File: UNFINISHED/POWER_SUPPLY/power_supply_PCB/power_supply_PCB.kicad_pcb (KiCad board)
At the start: 2 copper layers, 50 x 80 mm, 22 parts, among them J1 AC INPUT 12+12 1.5A, J2 OUT1, J3 OUT2, J4 OUT3, J5 OUT4, J6 OUT5, J7 OUT6, J8 OUT7, J9 OUT8, U1 LM7812_TO220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

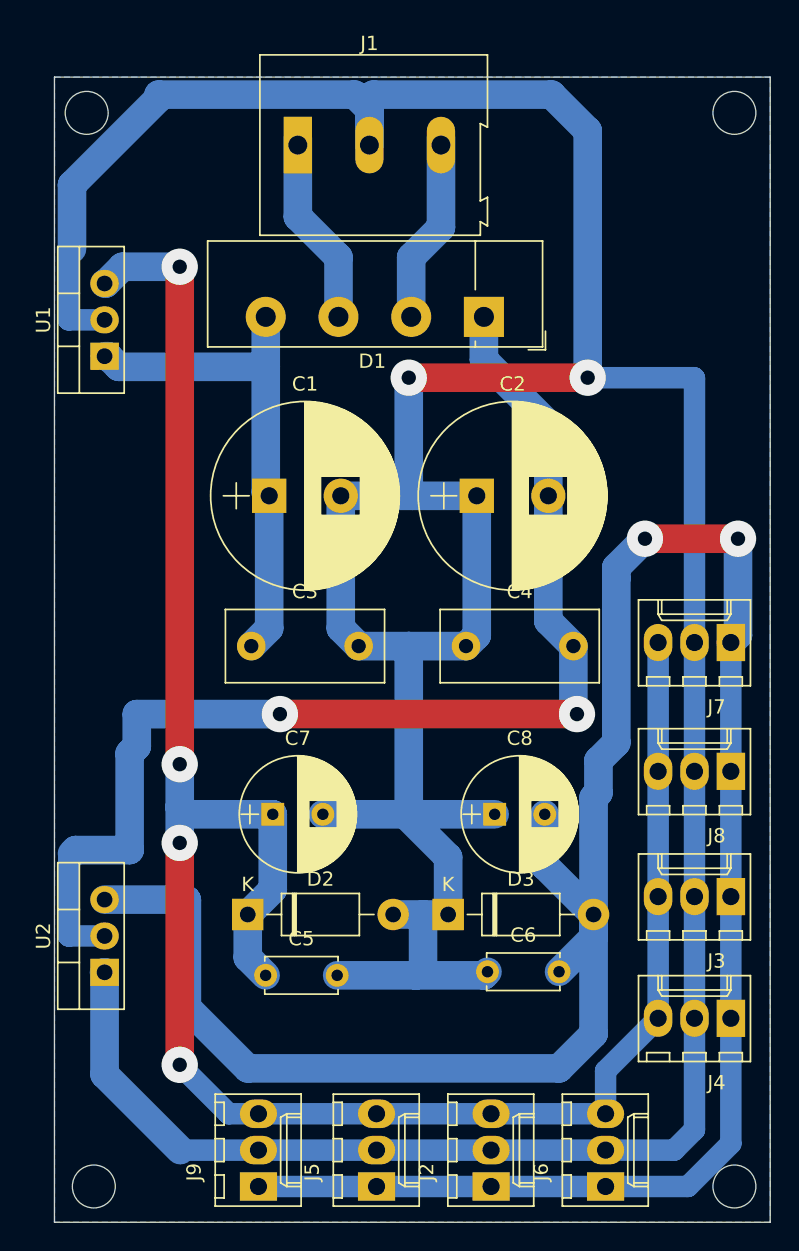
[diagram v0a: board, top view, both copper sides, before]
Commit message: power supply schematic OK
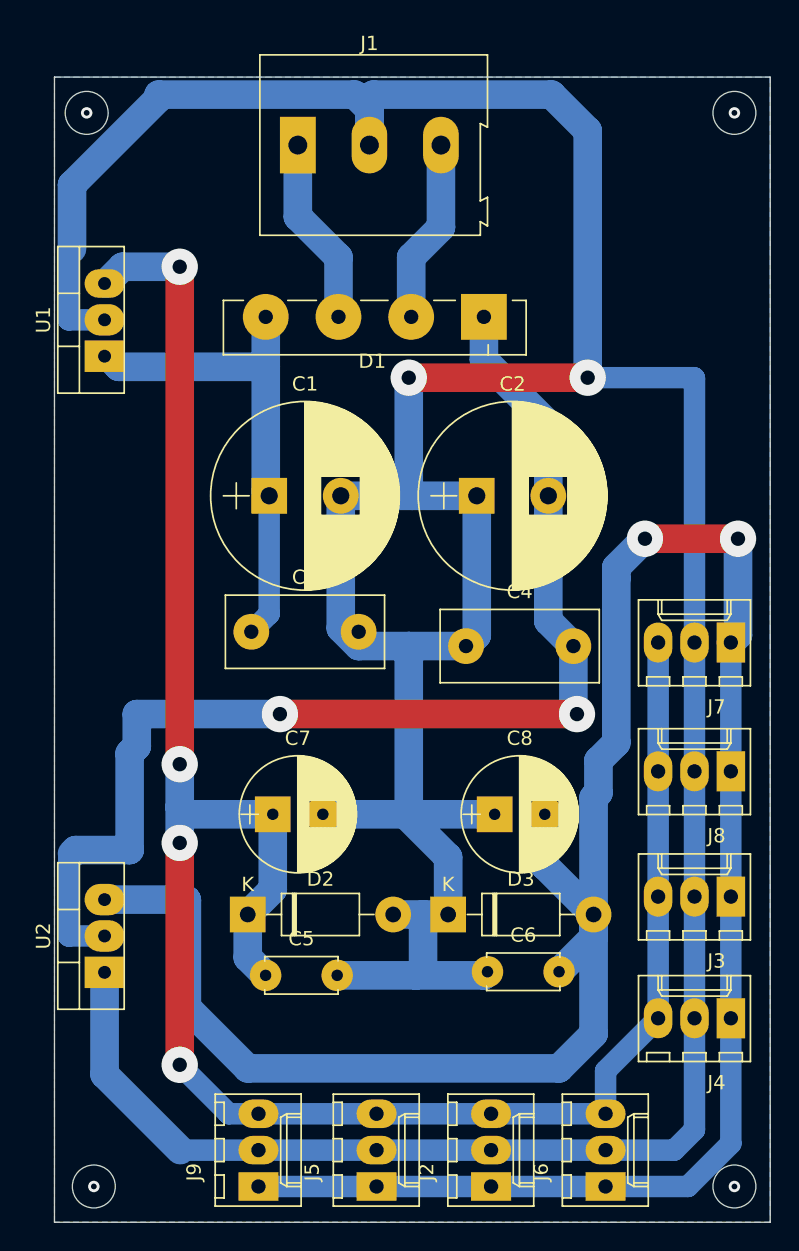
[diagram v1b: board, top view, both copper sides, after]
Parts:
- D1: footprint Diode_THT:Diode_Bridge_Vishay_KBU -> Diode_THT:Diode_Bridge_Vishay_GBL
- moved C3 1.00 mm to (63.8, 88.8)
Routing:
- net Net-(C1-Pad1): track 35.2 -> 34.2 mm
- net (no net): vias 0 -> 4
